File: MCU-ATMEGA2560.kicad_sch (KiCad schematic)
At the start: 41 parts, among them J10 Conn_01x10, J13 Conn_01x01_Pin, J14 Conn_01x01_Pin, J15 Conn_02x03_Odd_Even, J4 Conn_02x18_Odd_Even, J5 Conn_01x08, J6 Conn_01x08, J7 Conn_01x08, J8 Conn_01x08, J9 Conn_01x08, SW1 SW_MEC_5E, U1 LMV358, U4 MCU-ATMEGA2560-16AU_TQFP100_, U5 LP2985-3.3, U6 PMV48XP, Y1 CSTCE16M9V53-R0

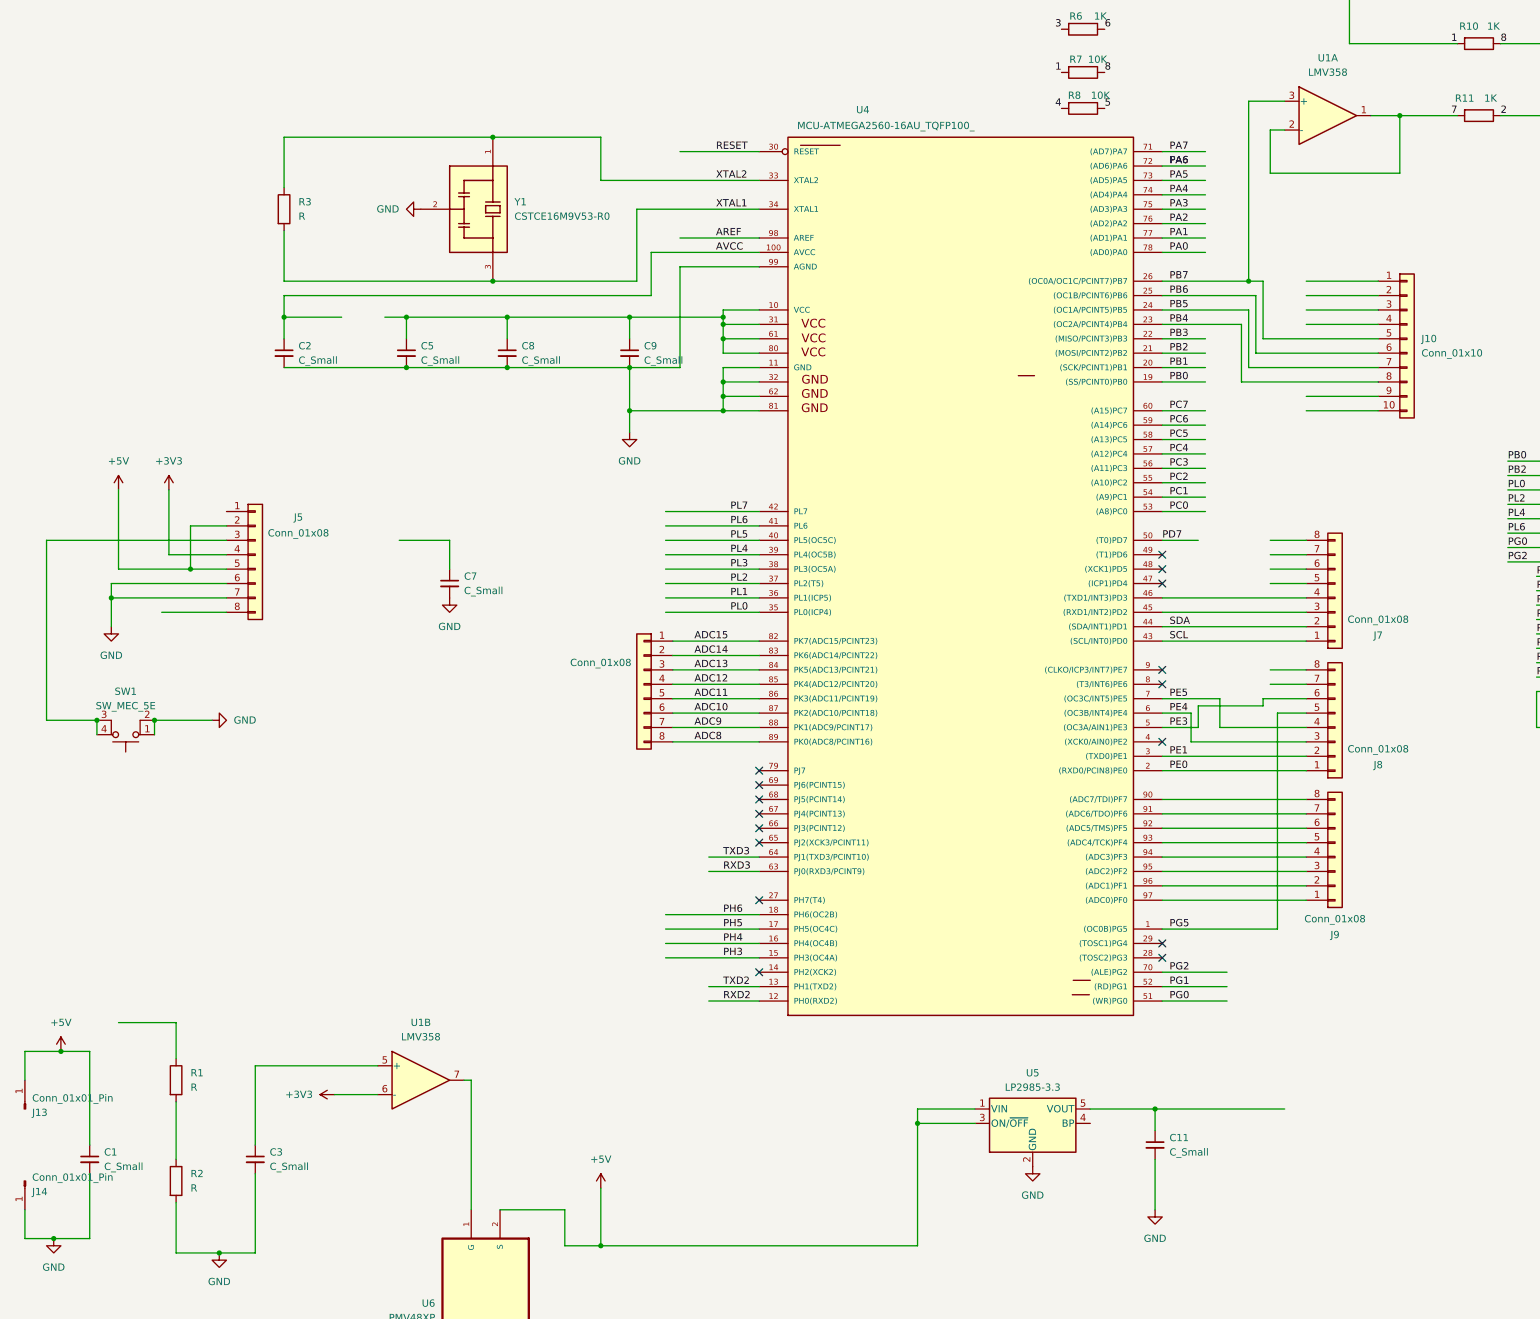
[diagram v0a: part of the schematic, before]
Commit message: finished the schematic without mpower supply
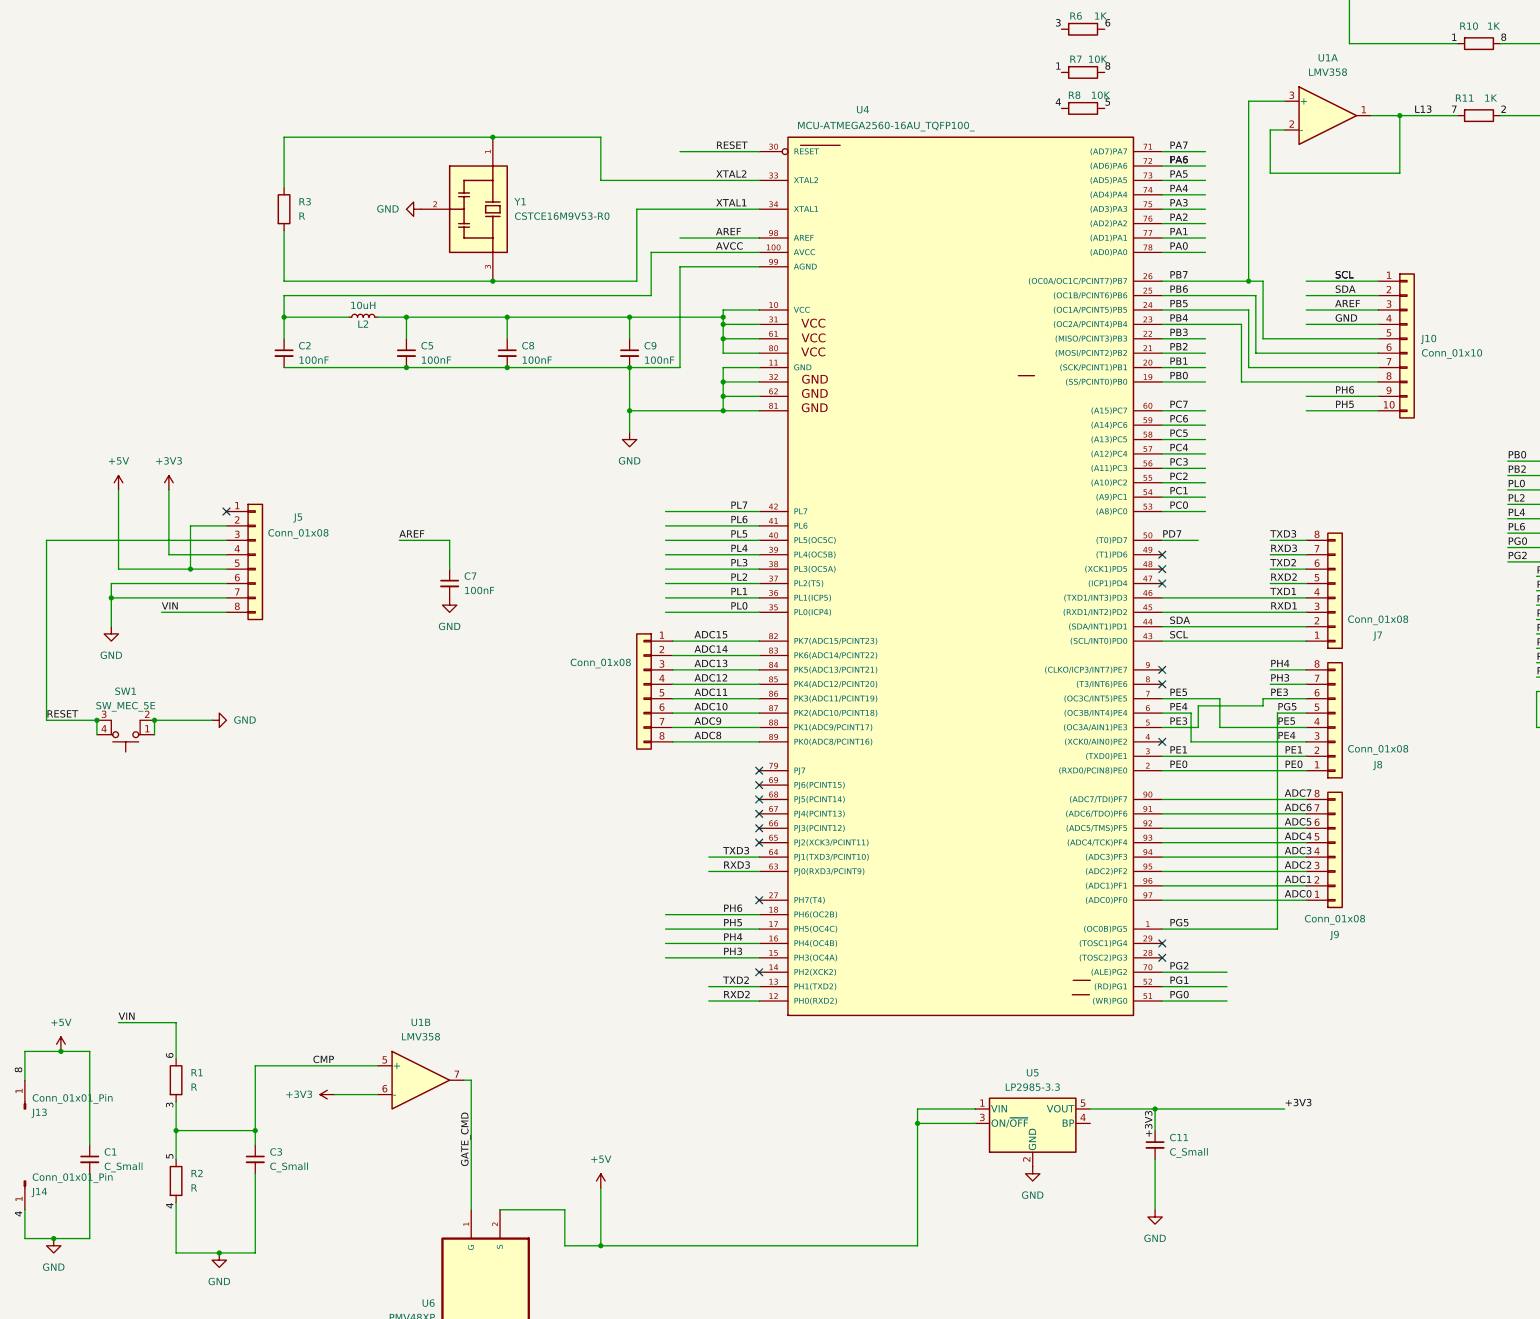
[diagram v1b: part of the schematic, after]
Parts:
- added L2: 10uH, symbol Device:L_Small
- C2, C5, C7, C8, C9: value C_Small -> 100nF
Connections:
- net 4 is gone; now on net GND: R8.2
- net 5 is gone; now on net 3: R8.1
- net 8 is gone; now on net +5V: D4.2 (A), R10.1, R7.1
- net PE5 is gone; now on net PE4: J8.4 (Pin_4), U4.7 ((OC3C/INT5)PE5)
- net PG5 is gone; now on net PE4: J8.5 (Pin_5), U4.1 ((OC0B)PG5)
- net +3V3: now also C11.1, U5.5 (VOUT)
- net +5V: now also J5.3 (Pin_3), J5.8 (Pin_8), R1.1, SW1.3 (K), SW1.4 (A)
- net 2: now also J10.1 (Pin_1)
- net 3: now also C3.1, J10.2 (Pin_2), R1.2, R2.1, U1.5 (+)
- net AREF: now also C7.1, J10.3 (Pin_3)
- net AVCC: now also L2.1
- net GND: now also J10.4 (Pin_4)
- net PH3: now also J8.7 (Pin_7)
- net PH4: now also J8.8 (Pin_8)
- net PH5: now also J10.10 (Pin_10)
- net PH6: now also J10.9 (Pin_9)
- net RXD2: now also J7.5 (Pin_5)
- net RXD3: now also J7.7 (Pin_7)
- net TXD2: now also J7.6 (Pin_6)
- net TXD3: now also J7.8 (Pin_8)
- net at C5.1, C8.1, C9.1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: now also L2.2
- net GATE_CMD: now reaches U1.7, U6.1 (G)
- net RXD1: now reaches J7.3 (Pin_3), U4.45 ((RXD1/INT2)PD2)
- net TXD1: now reaches J7.4 (Pin_4), U4.46 ((TXD1/INT3)PD3)
- net ADC7: now reaches J9.8 (Pin_8), U4.90 ((ADC7/TDI)PF7)
- net ADC6: now reaches J9.7 (Pin_7), U4.91 ((ADC6/TDO)PF6)
- net ADC5: now reaches J9.6 (Pin_6), U4.92 ((ADC5/TMS)PF5)
- net ADC4: now reaches J9.5 (Pin_5), U4.93 ((ADC4/TCK)PF4)
- net ADC3: now reaches J9.4 (Pin_4), U4.94 ((ADC3)PF3)
- net ADC2: now reaches J9.3 (Pin_3), U4.95 ((ADC2)PF2)
- net ADC1: now reaches J9.2 (Pin_2), U4.96 ((ADC1)PF1)
- net ADC0: now reaches J9.1 (Pin_1), U4.97 ((ADC0)PF0)
- no-connect marks 16 -> 17

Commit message: my potential final schematic
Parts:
- C1, C3: value C_Small -> 100nF
- C11: value C_Small -> 1uF
- C12: value 22p -> 22pF
- R1, R2, R9: value R -> 10K
- R3: value R -> 1M
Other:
- company: (none) -> GEVITON ENTERPRISES LIMITED
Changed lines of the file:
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@@
 		(title "MCU-ATMEGA2560")
 		(date "2024-07-11")
+		(rev "0")
+		(company "GEVITON ENTERPRISES LIMITED")
 	)
 	(junction
@@
 	(wire
 		(pts
-			(xy 388.62 41.91) (xy 388.62 49.53)
-		)
-		(stroke
-			(width 0)
-			(type default)
-		)
-	)
-	(wire
-		(pts
 			(xy 243.84 153.67) (xy 243.84 152.4)
 		)
@@
 			)
 		)
-		(property "Value" "C_Small"
+		(property "Value" "100nF"
 			(at 39.37 234.9562 0)
 			(effects
@@
 			)
 		)
-		(property "Value" "R"
+		(property "Value" "10K"
 			(at 54.61 220.9799 0)
 			(effects
@@
 			)
 		)
-		(property "Value" "R"
+		(property "Value" "1M"
 			(at 73.66 67.3099 0)
 			(effects
@@
 			)
 		)
-		(property "Value" "22p"
+		(property "Value" "22pF"
 			(at 332.74 223.5262 0)
 			(effects
@@
 		(on_board yes)
 		(dnp no)
-		(fields_autoplaced yes)
 		(property "Reference" "C3"
 			(at 68.58 232.4162 0)
@@
 			)
 		)
-		(property "Value" "C_Small"
-			(at 68.58 234.9562 0)
+		(property "Value" "100nF"
+			(at 68.58 234.95 0)
 			(effects
 				(font
@@
 		(on_board yes)
 		(dnp no)
-		(fields_autoplaced yes)
 		(property "Reference" "R9"
-			(at 349.25 203.1999 0)
+			(at 340.868 202.946 0)
 			(effects
 				(font
@@
 			)
 		)
-		(property "Value" "R"
-			(at 349.25 205.7399 0)
+		(property "Value" "10K"
+			(at 344.17 205.74 0)
 			(effects
 				(font
 					(size 1.27 1.27)
 				)
-				(justify left)
+				(justify right)
 			)
 		)
@@
 			)
 		)
-		(property "Value" "C_Small"
+		(property "Value" "1uF"
 			(at 227.33 232.4162 0)
 			(effects
@@
 			)
 		)
-		(property "Value" "R"
+		(property "Value" "10K"
 			(at 54.61 238.7599 0)
 			(effects

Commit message: remaining with mh2029, the two connectors to finish footprint assignment
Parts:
- C1, C11, C12, C2, C3, C5, C7, C8, C9: footprint (none) -> Capacitor_SMD:C_0402_1005Metric_Pad0.74x0.62mm_HandSolder
- CR1: footprint DIODE_CD1206-S01575_BRN -> CD1206_S01575:DIODE_CD1206-S01575_BRN
- D4, D5: footprint (none) -> LED_SMD:LED_0201_0603Metric_Pad0.64x0.40mm_HandSolder
- J10: footprint (none) -> Connector_PinSocket_1.00mm:PinSocket_1x10_P1.00mm_Vertical
- J15: footprint (none) -> Connector_PinHeader_1.00mm:PinHeader_2x03_P1.00mm_Vertical
- J4: footprint (none) -> Connector_PinSocket_1.27mm:PinSocket_2x18_P1.27mm_Vertical
- J5, J6, J7, J8, J9: footprint (none) -> Connector_PinSocket_1.00mm:PinSocket_1x08_P1.00mm_Vertical
- L2: footprint (none) -> Inductor_SMD:L_0201_0603Metric_Pad0.64x0.40mm_HandSolder
- R1, R10, R11, R12, R13, R2, R4, R5, R6, R7, R8, R9: footprint (none) -> Resistor_SMD:R_0201_0603Metric_Pad0.64x0.40mm_HandSolder
- R3: footprint (none) -> Resistor_SMD:R_0201_0603Metric
- SW1: footprint (none) -> Button_Switch_SMD:SW_MEC_5GSH9
- U1: footprint (none) -> Package_SO:MSOP-8-1EP_3x3mm_P0.65mm_EP2.5x3mm_Mask1.73x2.36mm_ThermalVias
- U4: footprint MCU-ATMEGA2560-16AU_TQFP100_:TQFP100-0.5-14X14MM -> MCU-ATMEGA2560-16AU_TQFP100:TQFP100-0.5-14X14MM
- Y1: footprint CSTCE16M9V53-R0:OSC_CSTCE16M9V53-R0 -> CSTCE16M9V53_R0:OSC_CSTCE16M9V53-R0
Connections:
- net +5V: now also R4.2
- net 3: now also R4.1
- net USBVCC: now reaches U6.3 (D)
- no-connect marks 17 -> 18

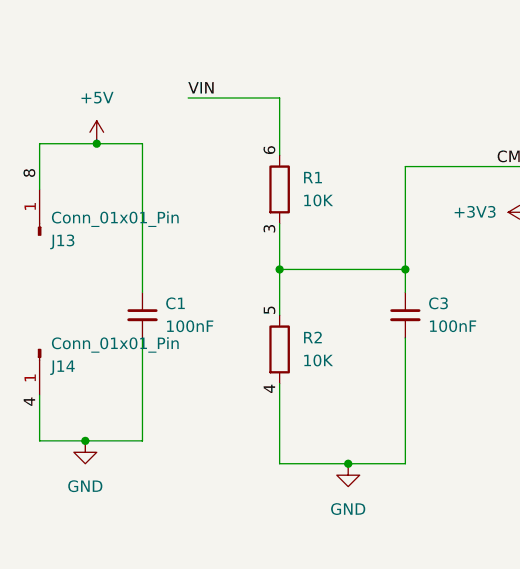
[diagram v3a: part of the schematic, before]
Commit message: finished editing the schematic and assigning footprints
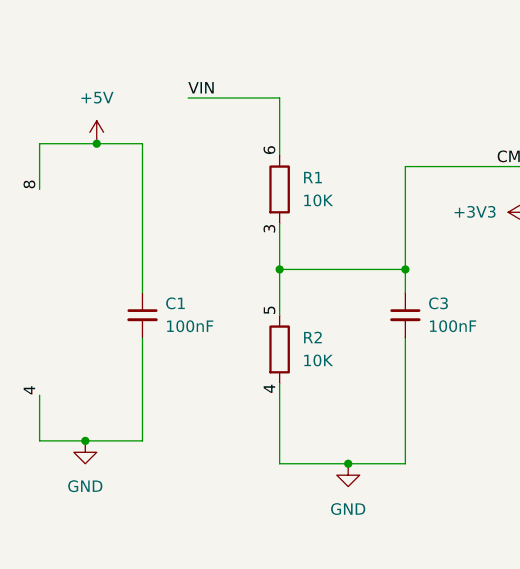
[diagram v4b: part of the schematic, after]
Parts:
- removed J13, J14: Conn_01x01_Pin, symbol Connector:Conn_01x01_Pin
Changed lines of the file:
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@@
 	)
 	(label "4"
-		(at 25.4 243.84 90)
+		(at 25.4 242.57 90)
 		(fields_autoplaced yes)
 		(effects
@@
 	)
 	(label "8"
-		(at 25.4 218.44 90)
+		(at 25.4 219.71 90)
 		(fields_autoplaced yes)
 		(effects
@@
 	)
 	(symbol
-		(lib_id "Connector:Conn_01x01_Pin")
-		(at 25.4 237.49 90)
-		(mirror x)
-		(unit 1)
-		(exclude_from_sim no)
-		(in_bom yes)
-		(on_board yes)
-		(dnp no)
-		(property "Reference" "J14"
-			(at 26.67 239.3951 90)
-			(effects
-				(font
-					(size 1.27 1.27)
-				)
-				(justify right)
-			)
-		)
-		(property "Value" "Conn_01x01_Pin"
-			(at 26.67 236.8551 90)
-			(effects
-				(font
-					(size 1.27 1.27)
-				)
-				(justify right)
-			)
-		)
-		(property "Footprint" ""
-			(at 25.4 237.49 0)
-			(effects
-				(font
-					(size 1.27 1.27)
-				)
-				(hide yes)
-			)
-		)
-		(property "Datasheet" "~"
-			(at 25.4 237.49 0)
-			(effects
-				(font
-					(size 1.27 1.27)
-				)
-				(hide yes)
-			)
-		)
-		(property "Description" "Generic connector, single row, 01x01, script generated"
-			(at 25.4 237.49 0)
-			(effects
-				(font
-					(size 1.27 1.27)
-				)
-				(hide yes)
-			)
-		)
-		(pin "1"
-		)
-		(instances
-			(project "arduino-mega-2560"
-				(path "/01593c05-32ee-43cc-9d3f-a6fed62a39f4/f9bc6889-35cb-482b-9d74-3324f3dce8d7"
-					(reference "J14")
-					(unit 1)
-				)
-			)
-		)
-	)
-	(symbol
 		(lib_id "power:GND")
 		(at 326.39 101.6 90)
@@
 					(unit 1)
 				)
-			)
-		)
-	)
-	(symbol
-		(lib_id "Connector:Conn_01x01_Pin")
-		(at 25.4 224.79 270)
-		(mirror x)
-		(unit 1)
-		(exclude_from_sim no)
-		(in_bom yes)
-		(on_board yes)
-		(dnp no)
-		(property "Reference" "J13"
-			(at 26.67 225.4251 90)
-			(effects
-				(font
-					(size 1.27 1.27)
-				)
-				(justify left)
-			)
-		)
-		(property "Value" "Conn_01x01_Pin"
-			(at 26.67 222.8851 90)
-			(effects
-				(font
-					(size 1.27 1.27)
-				)
-				(justify left)
-			)
-		)
-		(property "Footprint" ""
-			(at 25.4 224.79 0)
-			(effects
-				(font
-					(size 1.27 1.27)
-				)
-				(hide yes)
-			)
-		)
-		(property "Datasheet" "~"
-			(at 25.4 224.79 0)
-			(effects
-				(font
-					(size 1.27 1.27)
-				)
-				(hide yes)
-			)
-		)
-		(property "Description" "Generic connector, single row, 01x01, script generated"
-			(at 25.4 224.79 0)
-			(effects
-				(font
-					(size 1.27 1.27)
-				)
-				(hide yes)
-			)
-		)
-		(pin "1"
-		)
-		(instances
-			(project ""
-				(path "/01593c05-32ee-43cc-9d3f-a6fed62a39f4/f9bc6889-35cb-482b-9d74-3324f3dce8d7"
-					(reference "J13")
-					(unit 1)
-				)

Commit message: good progress
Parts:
- SW1: footprint Button_Switch_SMD:SW_MEC_5GSH9 -> Button_Switch_SMD:SW_Push_1P1T_NO_CK_KSC6xxJ
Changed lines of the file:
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@@
 			)
 		)
-		(property "Footprint" "Button_Switch_SMD:SW_MEC_5GSH9"
+		(property "Footprint" "Button_Switch_SMD:SW_Push_1P1T_NO_CK_KSC6xxJ"
 			(at 43.18 163.83 0)
 			(effects

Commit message: almost final
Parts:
- CR1: footprint CD1206_S01575:DIODE_CD1206-S01575_BRN -> Diode_SMD:D_0603_1608Metric
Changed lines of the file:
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@@
 			)
 		)
-		(property "Footprint" "CD1206_S01575:DIODE_CD1206-S01575_BRN"
+		(property "Footprint" "Diode_SMD:D_0603_1608Metric"
 			(at 353.06 209.55 0)
 			(effects

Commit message: hardest trial
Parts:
- J4: footprint Connector_PinSocket_1.27mm:PinSocket_2x18_P1.27mm_Vertical -> Connector_PinSocket_2.00mm:PinSocket_2x18_P2.00mm_Vertical
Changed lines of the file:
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@@
 			)
 		)
-		(property "Footprint" "Connector_PinSocket_1.27mm:PinSocket_2x18_P1.27mm_Vertical"
+		(property "Footprint" "Connector_PinSocket_2.00mm:PinSocket_2x18_P2.00mm_Vertical"
 			(at 307.34 130.81 0)
 			(effects

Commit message: correction on pcb layout
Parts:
- J10: footprint Connector_PinSocket_1.00mm:PinSocket_1x10_P1.00mm_Vertical -> Connector_PinSocket_1.27mm:PinSocket_1x10_P1.27mm_Vertical
- J5, J6, J7, J8, J9: footprint Connector_PinSocket_1.00mm:PinSocket_1x08_P1.00mm_Vertical -> Connector_PinHeader_1.27mm:PinHeader_1x08_P1.27mm_Vertical
- U1: footprint Package_SO:MSOP-8-1EP_3x3mm_P0.65mm_EP2.5x3mm_Mask1.73x2.36mm_ThermalVias -> Package_SO:MSOP-8-1EP_3x3mm_P0.65mm_EP2.5x3mm_Mask1.73x2.36mm
- U4: footprint MCU-ATMEGA2560-16AU_TQFP100:TQFP100-0.5-14X14MM -> ATMEGA2560-16AU:QFP50P1600X1600X120-100N
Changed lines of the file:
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@@
 			)
 		)
-		(property "Footprint" "Connector_PinSocket_1.00mm:PinSocket_1x08_P1.00mm_Vertical"
+		(property "Footprint" "Connector_PinHeader_1.27mm:PinHeader_1x08_P1.27mm_Vertical"
 			(at 256.54 134.62 0)
 			(effects
@@
 			)
 		)
-		(property "Footprint" "Package_SO:MSOP-8-1EP_3x3mm_P0.65mm_EP2.5x3mm_Mask1.73x2.36mm_ThermalVias"
+		(property "Footprint" "Package_SO:MSOP-8-1EP_3x3mm_P0.65mm_EP2.5x3mm_Mask1.73x2.36mm"
 			(at 255.27 49.53 0)
 			(effects
@@
 			)
 		)
-		(property "Footprint" "Connector_PinSocket_1.00mm:PinSocket_1x08_P1.00mm_Vertical"
+		(property "Footprint" "Connector_PinHeader_1.27mm:PinHeader_1x08_P1.27mm_Vertical"
 			(at 256.54 157.48 0)
 			(effects
@@
 			)
 		)
-		(property "Footprint" "MCU-ATMEGA2560-16AU_TQFP100:TQFP100-0.5-14X14MM"
+		(property "Footprint" "ATMEGA2560-16AU:QFP50P1600X1600X120-100N"
 			(at 190.5 132.08 0)
 			(effects
@@
 			)
 		)
-		(property "Footprint" "Package_SO:MSOP-8-1EP_3x3mm_P0.65mm_EP2.5x3mm_Mask1.73x2.36mm_ThermalVias"
+		(property "Footprint" "Package_SO:MSOP-8-1EP_3x3mm_P0.65mm_EP2.5x3mm_Mask1.73x2.36mm"
 			(at 95.25 219.71 0)
 			(effects
@@
 			)
 		)
-		(property "Footprint" "Connector_PinSocket_1.00mm:PinSocket_1x08_P1.00mm_Vertical"
+		(property "Footprint" "Connector_PinHeader_1.27mm:PinHeader_1x08_P1.27mm_Vertical"
 			(at 256.54 180.34 0)
 			(effects
@@
 			)
 		)
-		(property "Footprint" "Connector_PinSocket_1.00mm:PinSocket_1x10_P1.00mm_Vertical"
+		(property "Footprint" "Connector_PinSocket_1.27mm:PinSocket_1x10_P1.27mm_Vertical"
 			(at 269.24 88.9 0)
 			(effects
@@
 			)
 		)
-		(property "Footprint" "Connector_PinSocket_1.00mm:PinSocket_1x08_P1.00mm_Vertical"
+		(property "Footprint" "Connector_PinHeader_1.27mm:PinHeader_1x08_P1.27mm_Vertical"
 			(at 134.62 149.86 0)
 			(effects
@@
 			)
 		)
-		(property "Footprint" "Connector_PinSocket_1.00mm:PinSocket_1x08_P1.00mm_Vertical"
+		(property "Footprint" "Connector_PinHeader_1.27mm:PinHeader_1x08_P1.27mm_Vertical"
 			(at 66.04 127 0)
 			(effects
